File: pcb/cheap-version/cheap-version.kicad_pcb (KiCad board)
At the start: 4 copper layers, 100 x 100 mm, 169 parts, among them J201 UART / 3V3 logic, J301 SHT4x / XH 2.50, J302 FLOAT / 3.5 mm, J401 HRO TF-01A, J501 FAN1 / 3.5 mm, J511 FAN2 / 3.5 mm, J521 PUMP 24V / 6W, J601 PTC + / switched - (3.5 mm), J711 LED +/- (return isolated), J721 LED +/- (return isolated), J731 LED +/- (return isolated), J901 24V IN (KF301-5.0-2P), Q501 AO3400A, Q511 AO3400A, Q521 AO3422, Q601 IRL2505, Q711 BSC146N10LS5, Q721 BSC146N10LS5, SW201 RESET, SW202 BOOT, U101 ST1S10PHR, U201 ESP32-WROOM-32E-N4, U301 PCF8563T/5, U601 IRS4427S, U700 SN74LVC1G08DBVR, U710 AL8853S-13, U720 AL8853S-13, U902 ST1S14PHR, Y301 32.768k 12.5pF

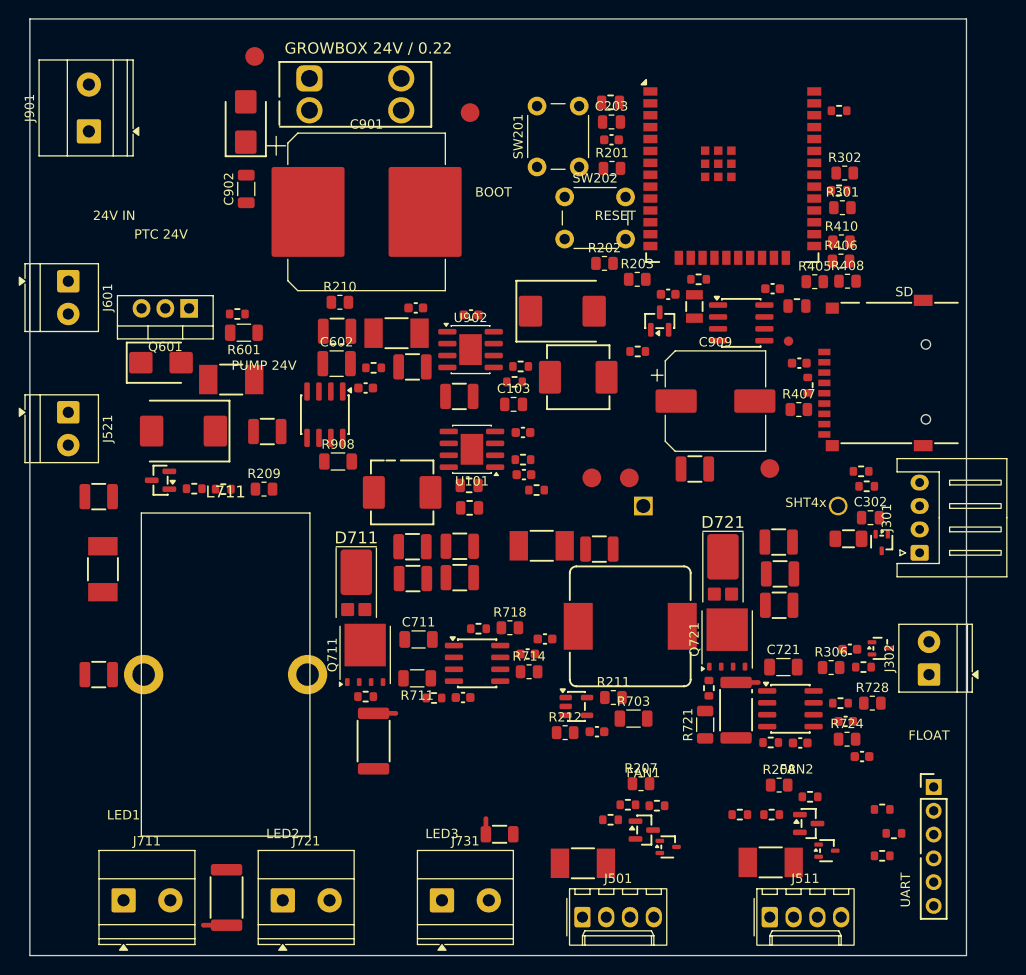
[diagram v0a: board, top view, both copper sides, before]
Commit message: cheap-version: save routing run 1 (Freerouting, no power pours yet)
Board with the first autorouter pass: GND plane + 99 ground ties from tools/route_power.py, then
tools/route_signals.py (Freerouting 2.4.1, 12 min, class widths MAIN24 2.0 / HEATER24 3.0 / LED_INPUT 2.0 /
SWITCH 1.5 mm). 961 router items, DRC: no clearance or short violations, 10 unconnected items, silk remarks
only. Not done yet: power pours for the 11.9 A trunk, loads, heater and boost nodes, the finish stage
(GND/3V3 fills), the last 10 connections. Also adds the copper viewer (export_view.py, view.py).

Co-Authored-By: Claude Sonnet 5.5 <noreply@anthropic.com>
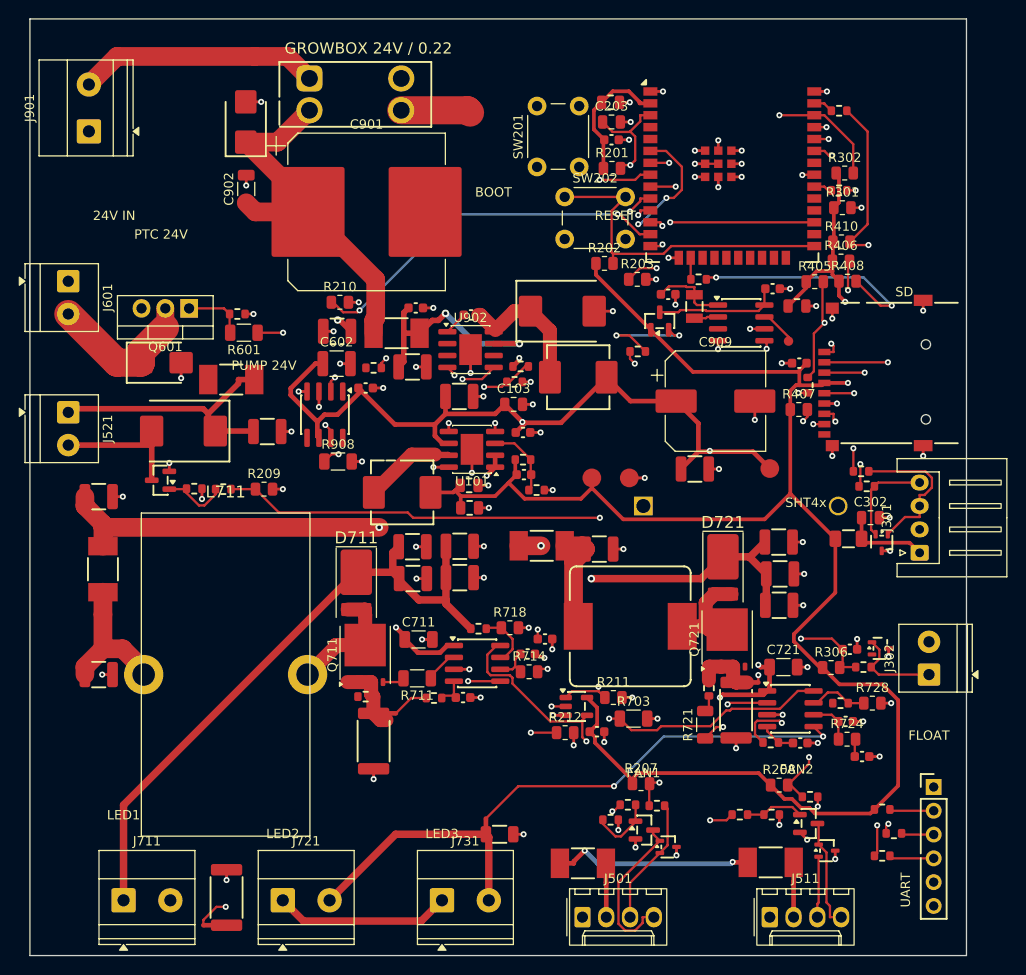
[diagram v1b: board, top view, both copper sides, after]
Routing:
- net +3V3: track 0.00 -> 226.9 mm, vias 0 -> 2
- net +12V: track 0.00 -> 209.9 mm, vias 0 -> 9
- net +24V: track 0.00 -> 199.9 mm, vias 0 -> 2
- net /MCU / ESP32/ESP_IO0: track 0.00 -> 125.8 mm
- net /MCU / ESP32/ESP_EN: track 0.00 -> 119.1 mm, vias 0 -> 1
- net GND: track 0.00 -> 117.4 mm, vias 0 -> 99
- net LIGHT_ENABLE: track 0.00 -> 93.7 mm, vias 0 -> 3
- net /LEDDrivers/LED2_OUT: track 0.00 -> 87.8 mm, vias 0 -> 1
- net PUMP_EN: track 0.00 -> 85.7 mm, vias 0 -> 2
- net /MCU / ESP32/UART_RX0: track 0.00 -> 80.5 mm, vias 0 -> 2
- net /MCU / ESP32/UART_TX0: track 0.00 -> 79.5 mm, vias 0 -> 2
- net FAN2_TACH: track 0.00 -> 77.8 mm, vias 0 -> 2
- net FAN1_TACH: track 0.00 -> 77.4 mm, vias 0 -> 3
- net FAN2_PWM: track 0.00 -> 72.3 mm, vias 0 -> 2
- net FAN1_PWM: track 0.00 -> 69.7 mm, vias 0 -> 2
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- added copper zone on In1.Cu, net GND
